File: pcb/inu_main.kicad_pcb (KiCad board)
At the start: 2 copper layers, 152.3 x 132.3 mm, 79 parts, among them CON1 MJ-4PP-9, CON2 MJ-4PP-9, J1 Conn_01x01, J2 Conn_01x03, J3 Conn_01x03, SW1 TactSW_2pin, U1 pro_micro

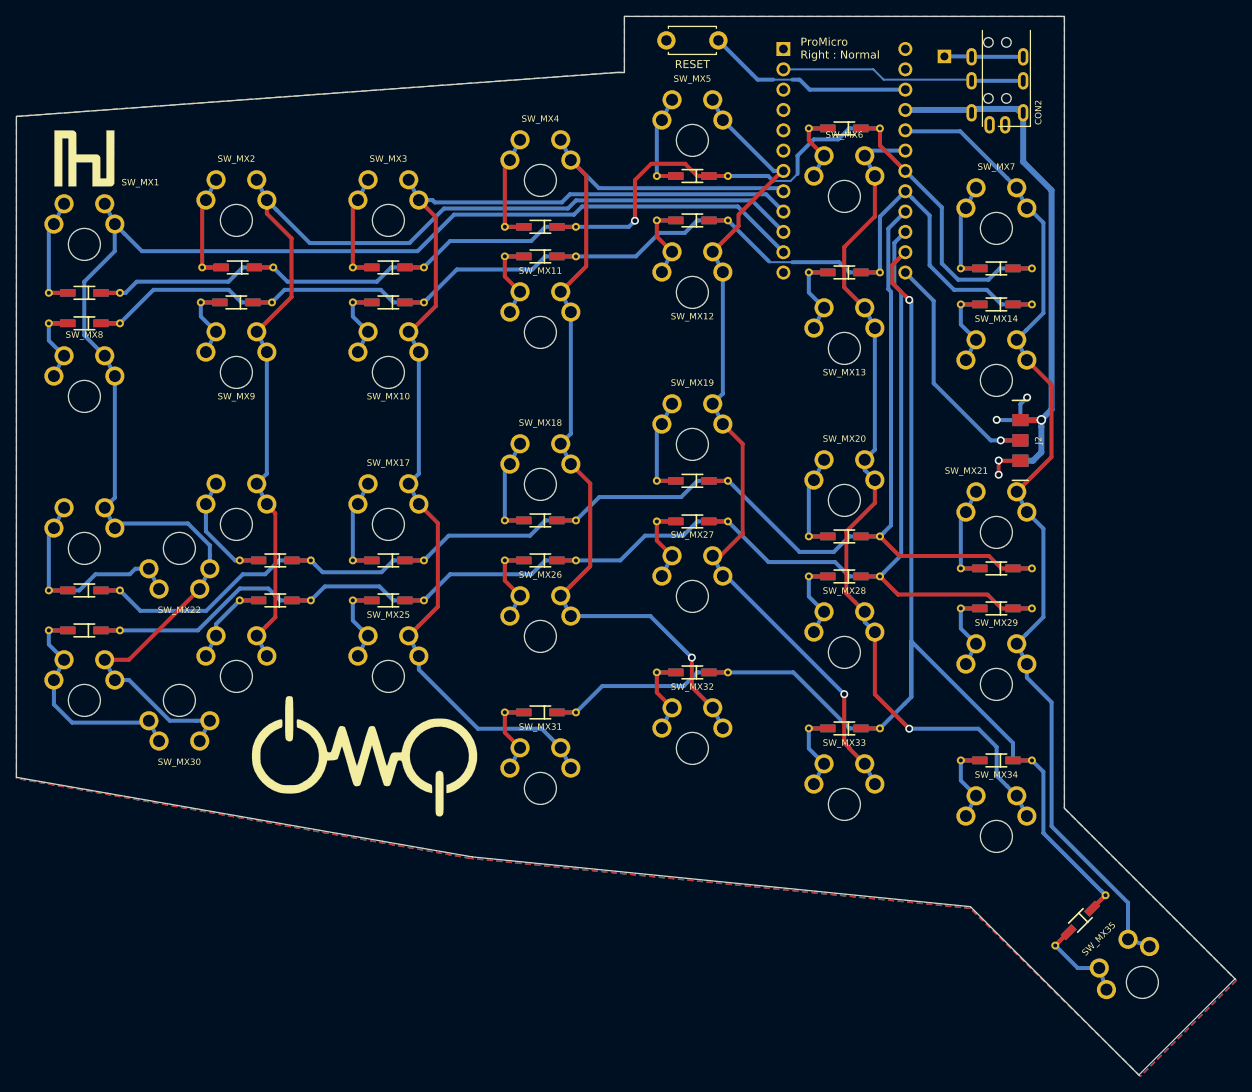
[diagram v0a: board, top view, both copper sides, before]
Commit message: add via to pcb
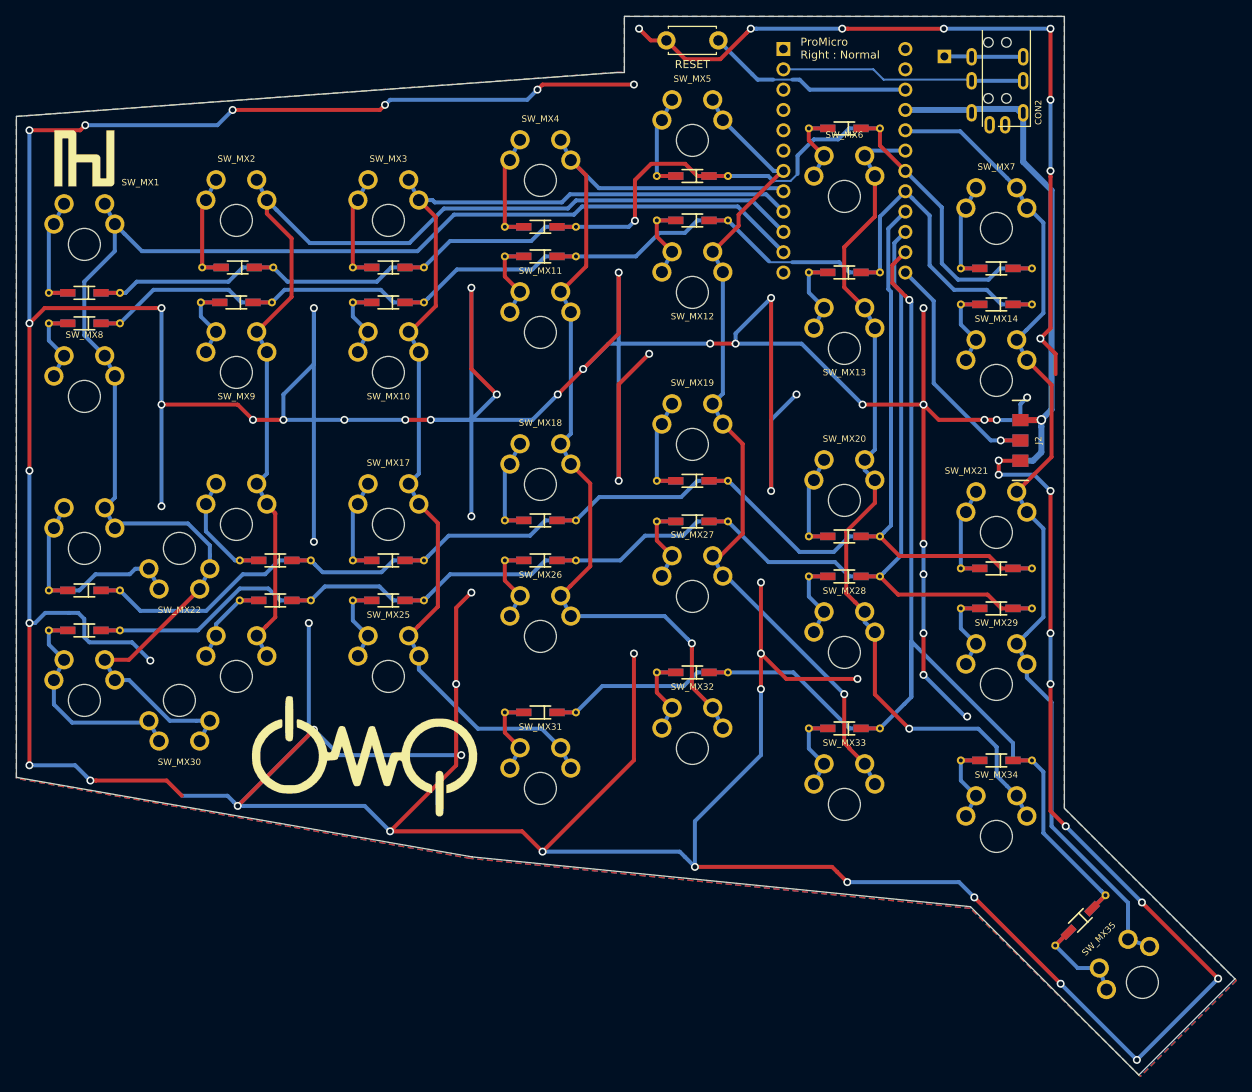
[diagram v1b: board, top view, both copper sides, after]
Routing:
- net GND: track 10.7 -> 1115.8 mm, vias 4 -> 80
- net /COL3: track 121.6 -> 122.6 mm

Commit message: fix silk on pcb
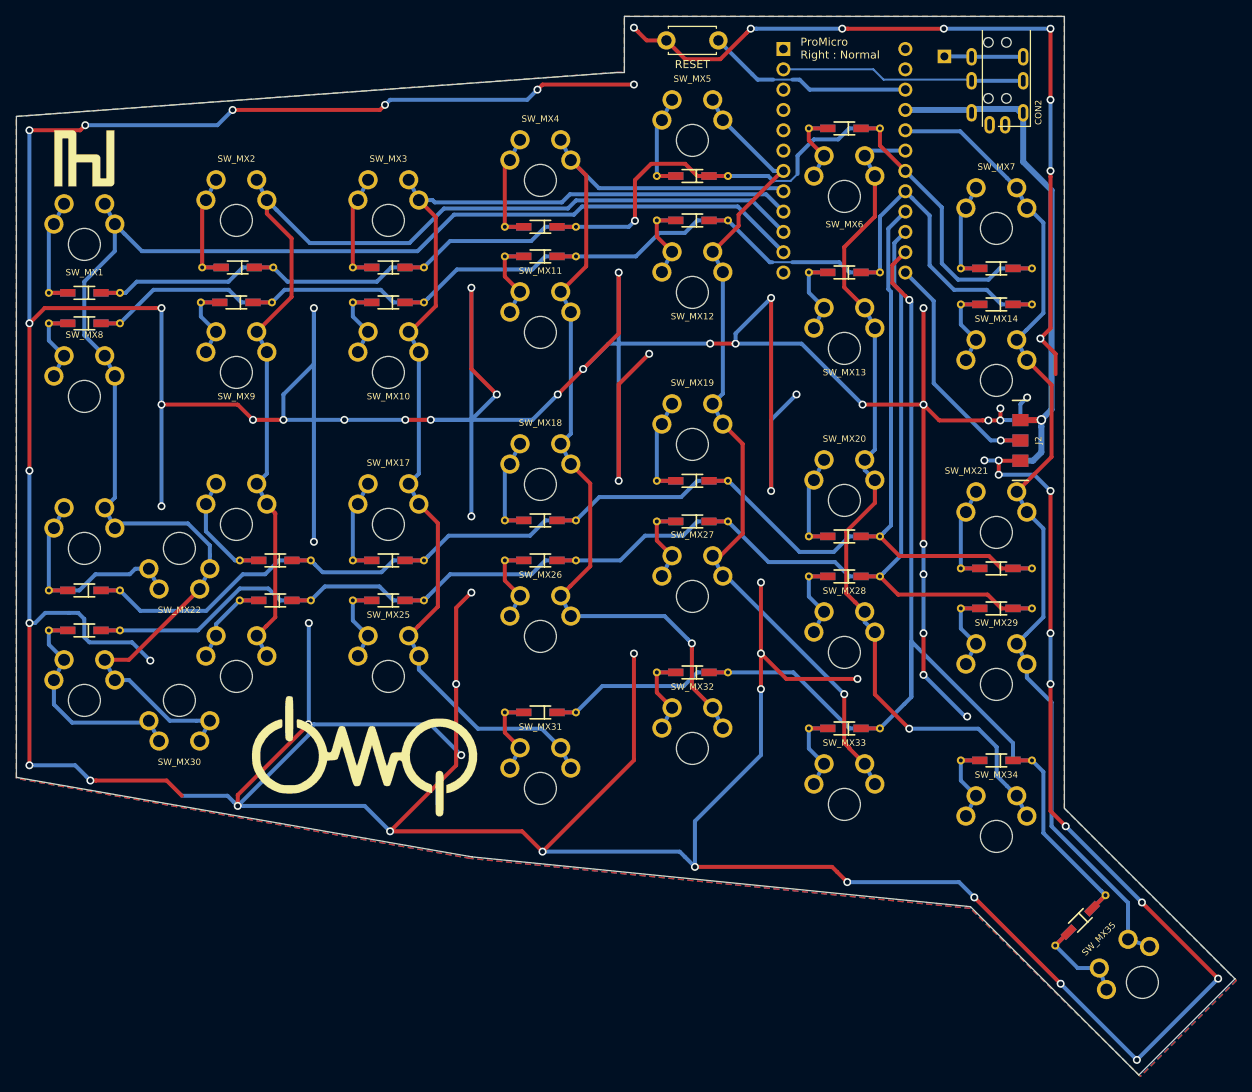
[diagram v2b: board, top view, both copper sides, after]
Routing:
- net GND: track 1115.8 -> 1121.1 mm, vias 80 -> 82
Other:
- board text added: "ergoinu An (Not Portable But Small) Ergonomic Split Keyboard Rev.1 (c) 2018, Takuya Urakawa / Dm9Records.com"
- board text removed: "ergoinu - (Not Portable) Ergonomic Split Keyboard main PCB / Rev.1 Alpha (c) 2018, Takuya Urakawa / Dm9Records.com"

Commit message: update pcb
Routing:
- net GND: track 1121.1 -> 22.3 mm, vias 82 -> 85

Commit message: pcb rev 1 final update
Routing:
- net /COL4: track 105.9 -> 106.9 mm
- net GND: vias 85 -> 87
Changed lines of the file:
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@@
     (thickness 1.6)
     (drawings 24)
-    (tracks 696)
+    (tracks 699)
     (zones 0)
     (modules 79)
@@
     (0 F.Cu signal)
     (31 B.Cu signal)
-    (32 B.Adhes user)
-    (33 F.Adhes user)
-    (34 B.Paste user)
-    (35 F.Paste user)
+    (32 B.Adhes user hide)
+    (33 F.Adhes user hide)
+    (34 B.Paste user hide)
+    (35 F.Paste user hide)
     (36 B.SilkS user)
     (37 F.SilkS user)
@@
     (40 Dwgs.User user)
     (41 Cmts.User user)
-    (42 Eco1.User user)
-    (43 Eco2.User user)
-    (44 Edge.Cuts user)
-    (45 Margin user)
+    (42 Eco1.User user hide)
+    (43 Eco2.User user hide)
+    (44 Edge.Cuts user hide)
+    (45 Margin user hide)
     (46 B.CrtYd user)
     (47 F.CrtYd user)
@@
     (pad_to_mask_clearance 0.2)
     (solder_mask_min_width 0.2)
-    (aux_axis_origin 153.5 24.5)
+    (aux_axis_origin 153.500598 24.499209)
     (visible_elements 7FFDFFFF)
     (pcbplotparams
-      (layerselection 0x010f0_80000001)
+      (layerselection 0x010f0_ffffffff)
       (usegerberextensions false)
       (usegerberattributes false)
@@
   (via (at 135.75 40) (size 1) (drill 0.6) (layers F.Cu B.Cu) (net 1))
   (via (at 149.5 54) (size 1) (drill 0.6) (layers F.Cu B.Cu) (net 1))
+  (via (at 68.58 100.33) (size 1) (drill 0.6) (layers F.Cu B.Cu) (net 1))
+  (via (at 30.48 106.68) (size 1) (drill 0.6) (layers F.Cu B.Cu) (net 1))
   (segment (start 141.95 36.55) (end 141.9 36.55) (width 0.75) (layer B.Cu) (net 2) (status 30))
   (segment (start 142.432 36.068) (end 141.95 36.55) (width 0.75) (layer B.Cu) (net 2) (status 30))
@@
   (segment (start 117.165 43.815) (end 118.38 43.815) (width 0.5) (layer B.Cu) (net 47) (status 20))
   (segment (start 110.81 37.46) (end 117.165 43.815) (width 0.5) (layer B.Cu) (net 47) (status 10))
-  (segment (start 112.776 50.684) (end 109.54 53.92) (width 0.5) (layer F.Cu) (net 47) (status 20))
-  (segment (start 112.776 49.276) (end 112.776 50.684) (width 0.5) (layer F.Cu) (net 47))
-  (segment (start 118.38 43.815) (end 118.237 43.815) (width 0.5) (layer F.Cu) (net 47) (status 30))
-  (segment (start 118.237 43.815) (end 112.776 49.276) (width 0.5) (layer F.Cu) (net 47) (status 10))
   (segment (start 110.81 71.65) (end 109.54 72.92) (width 0.5) (layer B.Cu) (net 47) (status 20))
   (segment (start 110.81 56.46) (end 110.81 71.65) (width 0.5) (layer B.Cu) (net 47) (status 10))
@@
   (segment (start 109.54 91.92) (end 110.81 94.46) (width 0.5) (layer B.Cu) (net 47) (status 30))
   (segment (start 128.54 117.92) (end 129.81 120.46) (width 0.5) (layer B.Cu) (net 47) (status 30))
+  (segment (start 111.18 53.92) (end 109.54 53.92) (width 0.5) (layer F.Cu) (net 47))
+  (segment (start 114.3 50.8) (end 111.18 53.92) (width 0.5) (layer F.Cu) (net 47))
+  (segment (start 114.3 47.752) (end 114.3 50.8) (width 0.5) (layer F.Cu) (net 47))
+  (segment (start 118.38 43.815) (end 118.237 43.815) (width 0.5) (layer F.Cu) (net 47))
+  (segment (start 118.237 43.815) (end 114.3 47.752) (width 0.5) (layer F.Cu) (net 47))
   (segment (start 129.185 41.275) (end 128.54 41.92) (width 0.5) (layer B.Cu) (net 48) (status 30))
   (segment (start 133.62 41.275) (end 129.185 41.275) (width 0.5) (layer B.Cu) (net 48) (status 30))
